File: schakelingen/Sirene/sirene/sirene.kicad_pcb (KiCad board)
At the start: 2 copper layers, 100 x 75 mm, 23 parts, among them Q1 BC557, Q2 BC547, Q3 BC557, Q4 BC557, Q5 TIP42

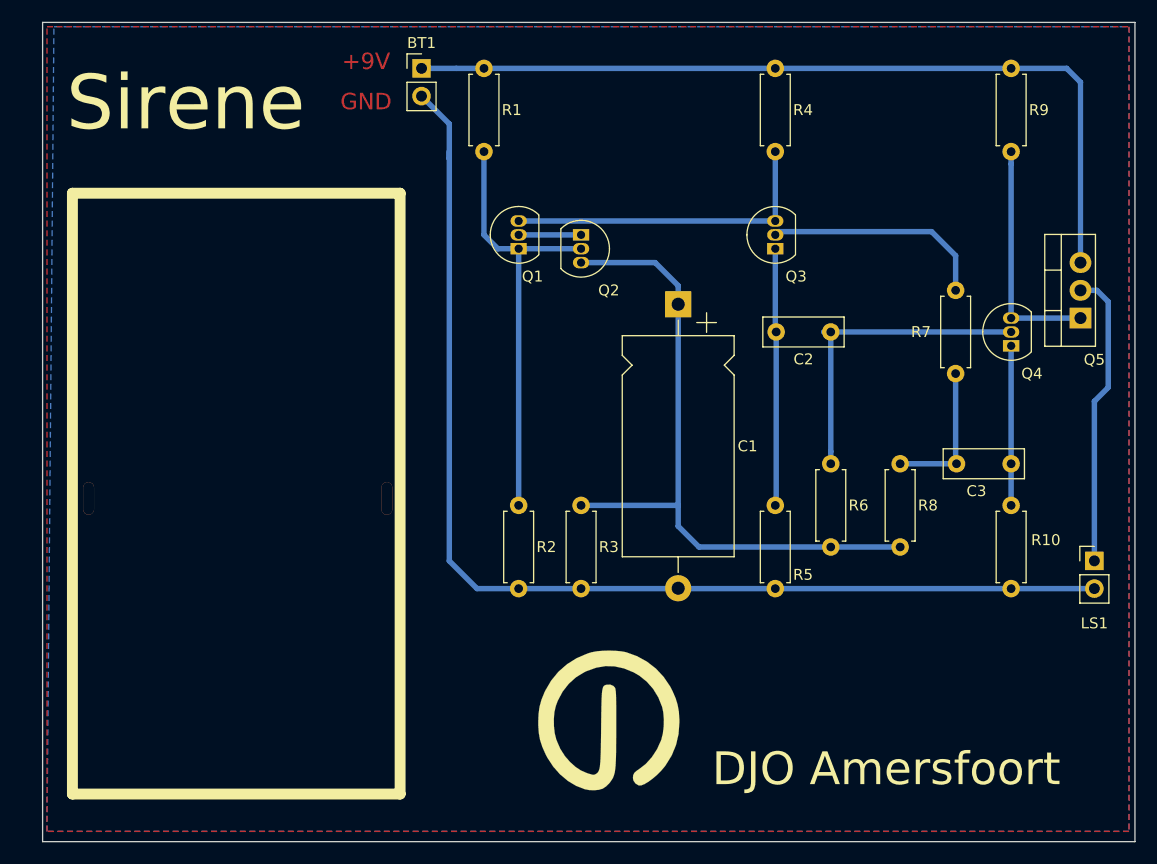
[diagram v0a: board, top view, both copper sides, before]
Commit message: Readme. 9V batterij in bibliotheek. Knipperlicht toegevoegd.
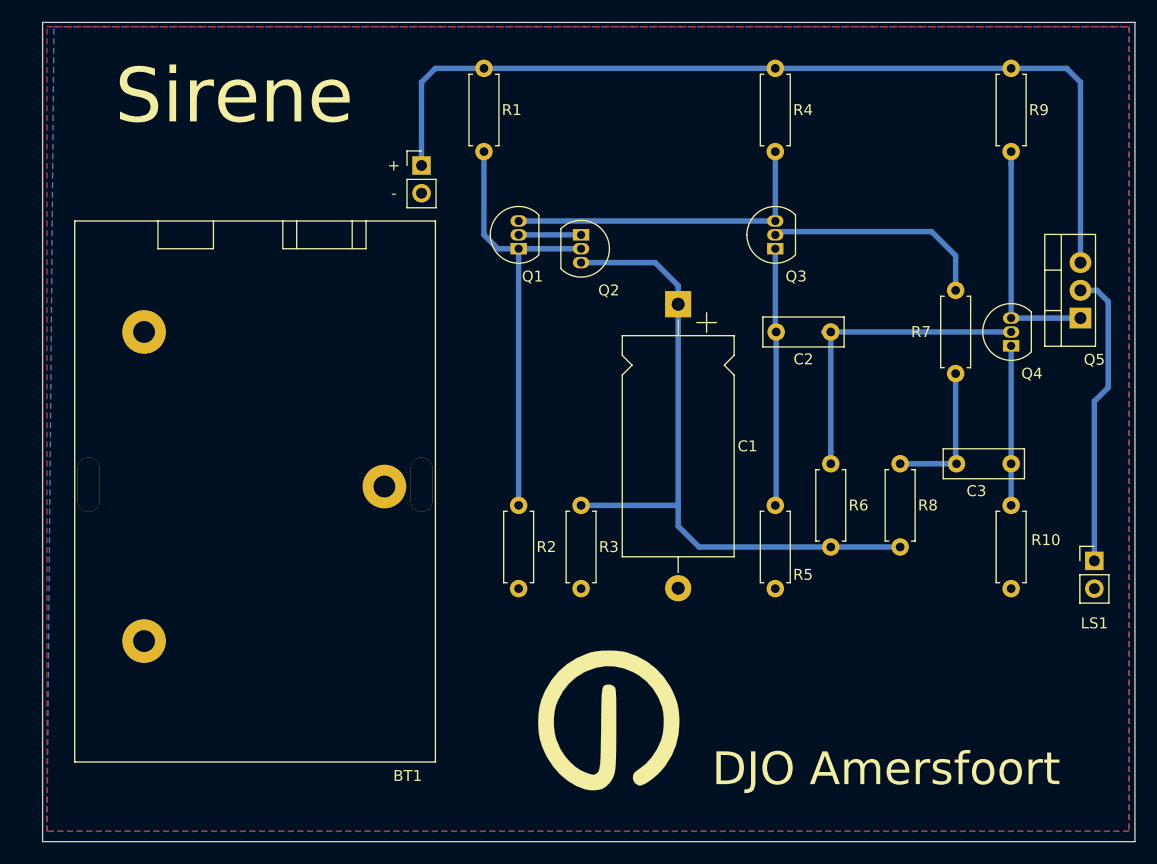
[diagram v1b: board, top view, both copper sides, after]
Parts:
- removed REF** (x2): Tiewrap hole, DJO_mechanical:Tiewrap hole
- BT1: footprint Connector_PinHeader_2.54mm:PinHeader_1x02_P2.54mm_Vertical -> 9v batterij:9v batterij
- moved BT1 41.0 mm to (44.5, 67.3)
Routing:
- net GND: track 104.3 -> 0.00 mm
- net Net-(BT1-Pad1): track 77.4 -> 85.4 mm
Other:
- board text removed: "+9V"
- board text removed: "GND"

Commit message: Footprint van sirene bijgewerkt voor handsolderen.
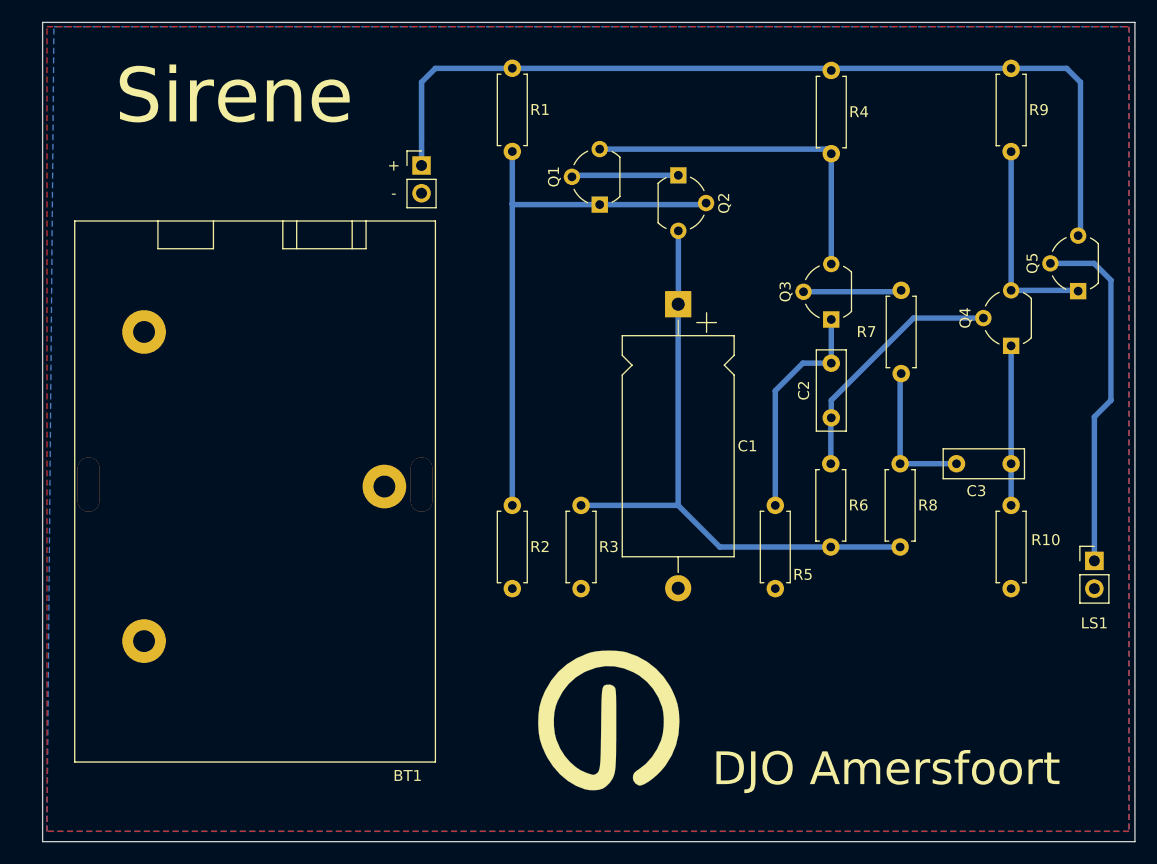
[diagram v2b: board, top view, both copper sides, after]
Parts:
- Q1, Q2, Q3, Q4: footprint Package_TO_SOT_THT:TO-92_Inline -> Package_TO_SOT_THT:TO-92_Wide
- Q5: footprint Package_TO_SOT_THT:TO-220-3_Vertical -> Package_TO_SOT_THT:TO-92_Wide
- moved Q2 10.4 mm to (83.2, 39.0)
- moved Q1 8.45 mm to (76.0, 41.7)
- moved Q3 8.26 mm to (97.2, 52.2)
- moved C2 7.86 mm to (97.2, 61.2), turned to 90 degrees
- moved R4 5.13 mm to (97.2, 29.4)
- moved R7 4.98 mm to (103.6, 57.1)
- moved R1 2.60 mm to (68.0, 29.2)
- moved Q5 2.48 mm to (119.8, 49.6)
- moved R2 0.58 mm to (68.0, 69.2)
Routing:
- net Net-(Q3-Pad2): track 20.7 -> 8.99 mm
- net Net-(Q1-Pad1): track 40.5 -> 50.2 mm
- net Net-(C2-Pad1): track 29.8 -> 22.9 mm
- net Net-(C1-Pad1): track 61.8 -> 56.0 mm
- net Net-(LS1-Pad1): track 27.2 -> 32.5 mm
- net Net-(Q1-Pad2): track 5.72 -> 9.80 mm
- net Net-(C2-Pad2): track 23.6 -> 20.8 mm
- net Net-(Q4-Pad3): track 21.6 -> 18.9 mm
- net Net-(BT1-Pad1): track 85.4 -> 83.2 mm
- net Net-(Q1-Pad3): track 30.5 -> 31.8 mm
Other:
- net class Default removed

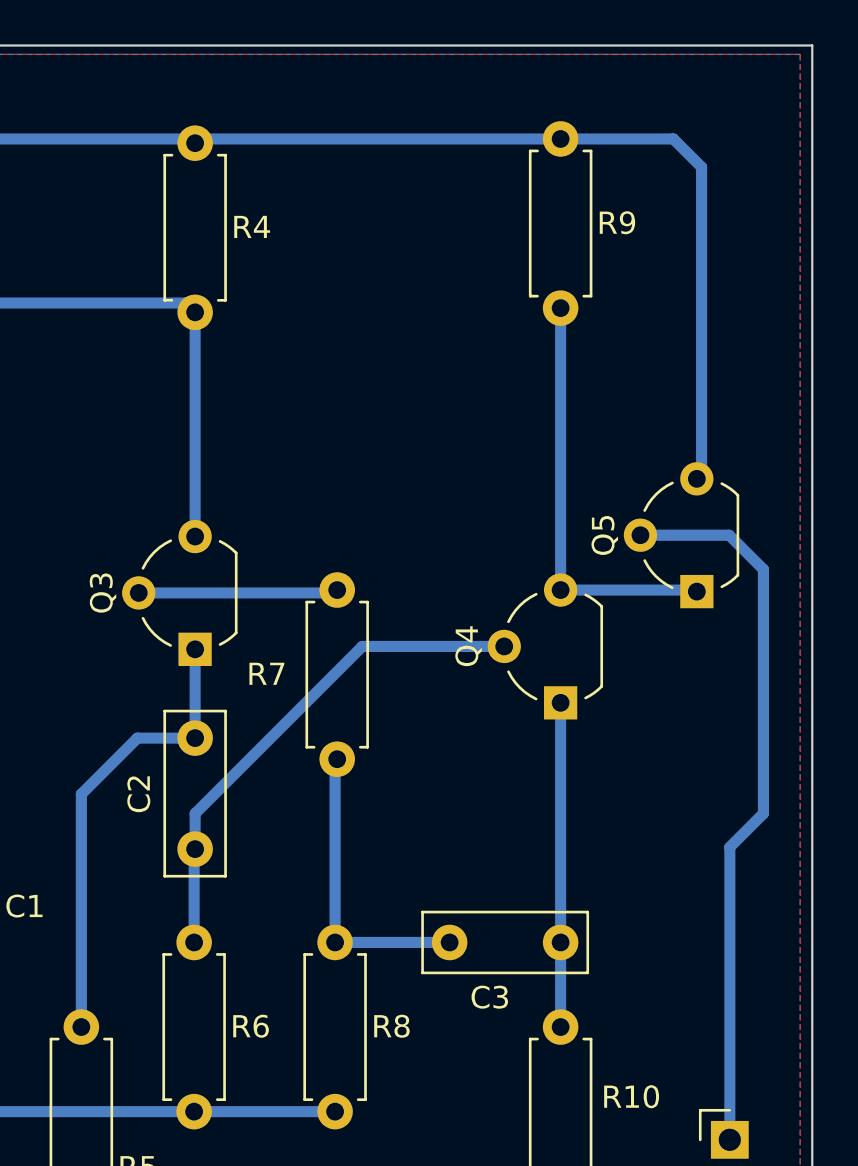
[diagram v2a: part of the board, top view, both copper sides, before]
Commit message: Footprint Q5 sirene veranderd naar TO-220
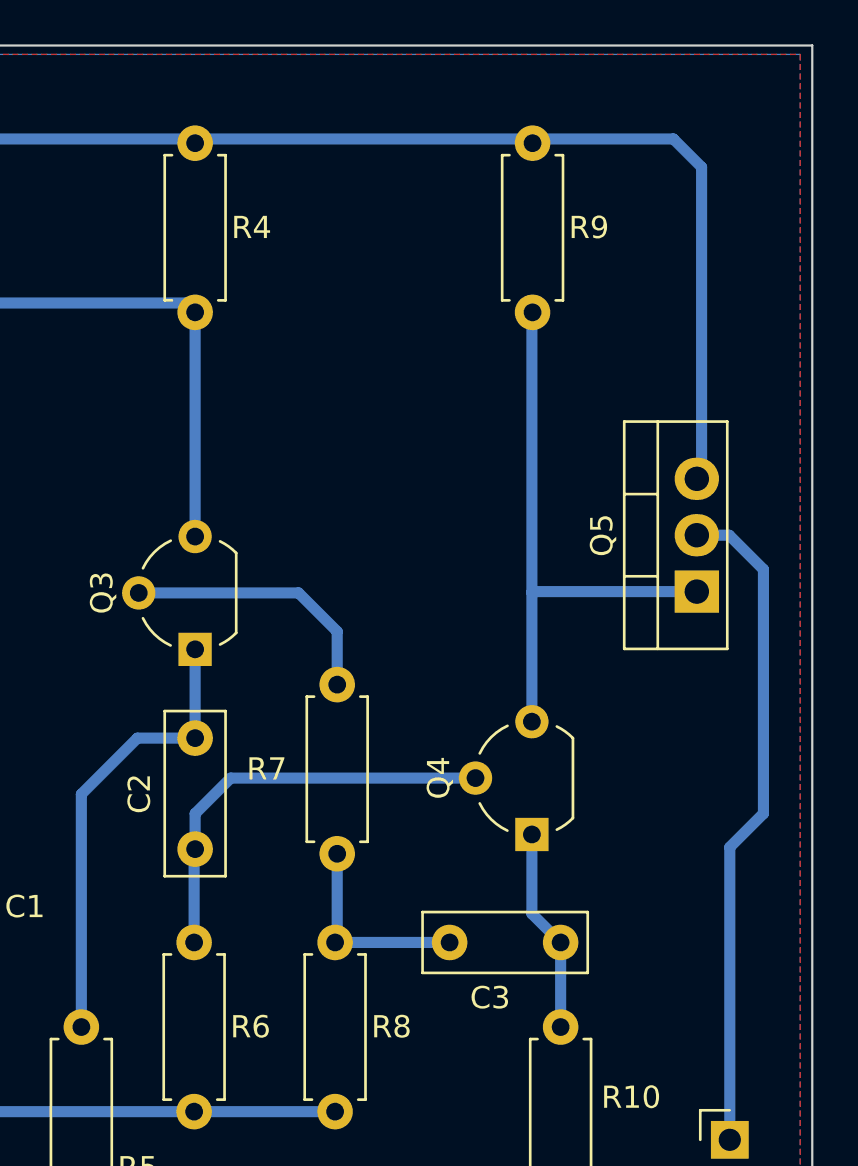
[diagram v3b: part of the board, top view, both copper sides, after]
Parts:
- Q5: footprint Package_TO_SOT_THT:TO-92_Wide -> Package_TO_SOT_THT:TO-220-3_Vertical
- moved Q4 6.07 mm to (112.4, 60.5)
- moved R7 4.26 mm to (103.6, 61.4)
- moved R9 1.28 mm to (112.4, 29.4)
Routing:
- net Net-(Q4-Pad3): track 18.9 -> 26.3 mm
- net Net-(C3-Pad1): track 14.6 -> 9.21 mm
- net Net-(C3-Pad2): track 13.6 -> 9.31 mm
- net Net-(C2-Pad1): track 22.9 -> 19.1 mm
- net Net-(Q3-Pad2): track 8.99 -> 12.1 mm
- net Net-(LS1-Pad1): track 32.5 -> 30.0 mm
